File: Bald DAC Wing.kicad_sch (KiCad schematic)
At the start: 50 parts, among them J1 PWR, J10 Ctrl Debug, J2 DAC_A_Out, J3 DAC_B_Out, J5 Z_Out, J6 Feather, J7 Data Debug Low, J9 Data Debug High, U1 AD5447, U2 AD8065ARTZ, U3 AD8065ARTZ, U4 74LVC574APWR, U5 74LVC574APWR, U6 74LVC1G04, U7 REF3425

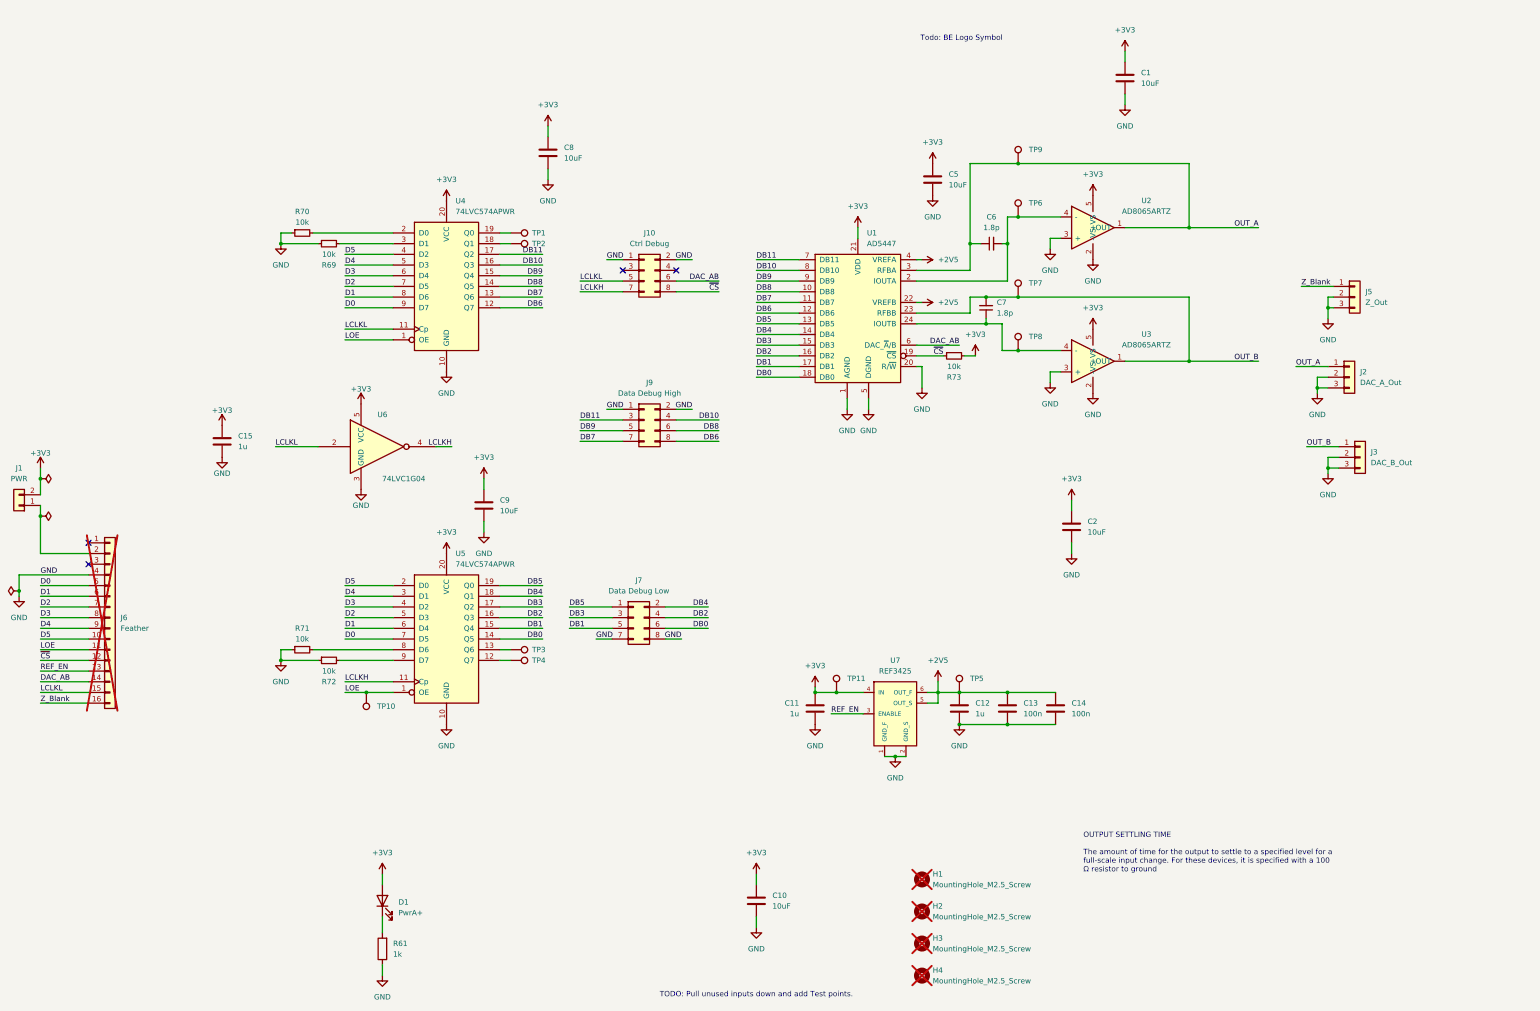
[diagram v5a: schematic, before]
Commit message: added BNCs for ABZ
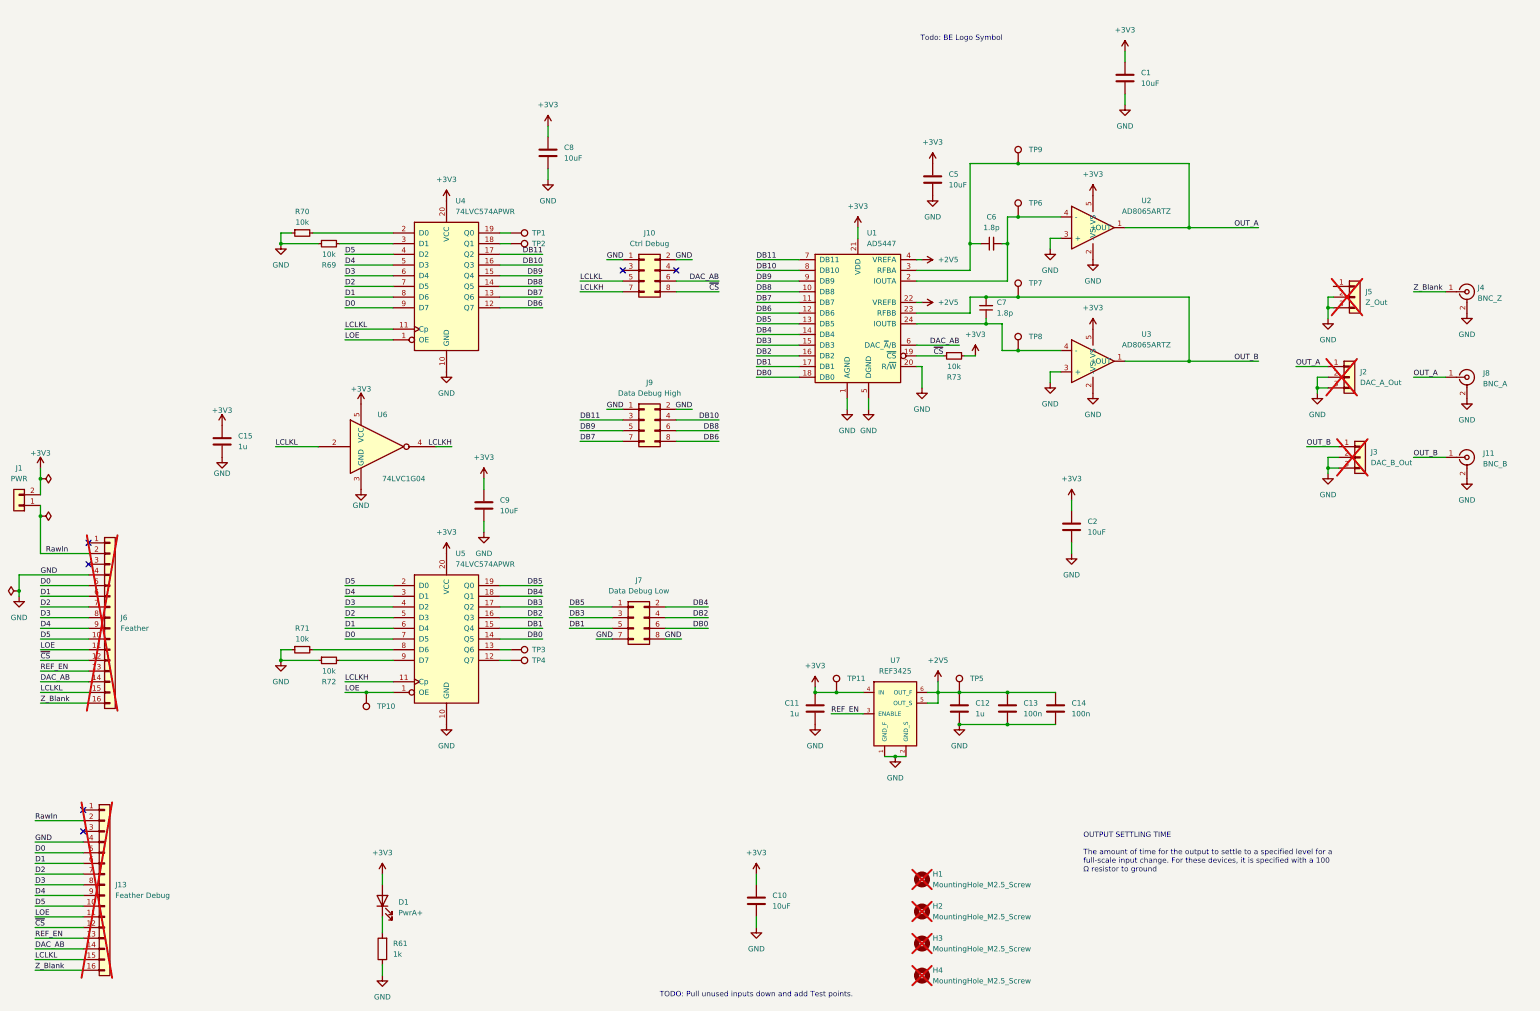
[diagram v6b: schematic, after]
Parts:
- added J11: BNC_B, My Libraries:Molex_73100-0105_BNC_RA, symbol Connector:Conn_Coaxial
- added J13: Feather Debug, Connector_PinSocket_2.54mm:PinSocket_1x16_P2.54mm_Vertical, symbol Connector_Generic:Conn_01x16
- added J4: BNC_Z, My Libraries:Molex_73100-0105_BNC_RA, symbol Connector:Conn_Coaxial
- added J8: BNC_A, My Libraries:Molex_73100-0105_BNC_RA, symbol Connector:Conn_Coaxial
- J2, J3, J5: now not fitted
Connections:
- net D0: now also J13.5 (Pin_5)
- net D1: now also J13.6 (Pin_6)
- net D2: now also J13.7 (Pin_7)
- net D3: now also J13.8 (Pin_8)
- net D4: now also J13.9 (Pin_9)
- net D5: now also J13.10 (Pin_10)
- net DAC_AB: now also J13.14 (Pin_14)
- net GND: now also J11.2 (Ext), J13.4 (Pin_4), J4.2 (Ext), J8.2 (Ext)
- net LCLKL: now also J13.15 (Pin_15)
- net LOE: now also J13.11 (Pin_11)
- net OUT_A: now also J8.1 (In)
- net OUT_B: now also J11.1 (In)
- net REF_EN: now also J13.13 (Pin_13)
- net Z_Blank: now also J13.16 (Pin_16), J4.1 (In); no longer J5.1 (Pin_1)
- net ~{CS}: now also J13.12 (Pin_12)
- net RawIn: now reaches J1.1 (Pin_1), J6.2 (Pin_2)
- net RawIn: now also J13.2 (Pin_2)
- no-connect marks 4 -> 6

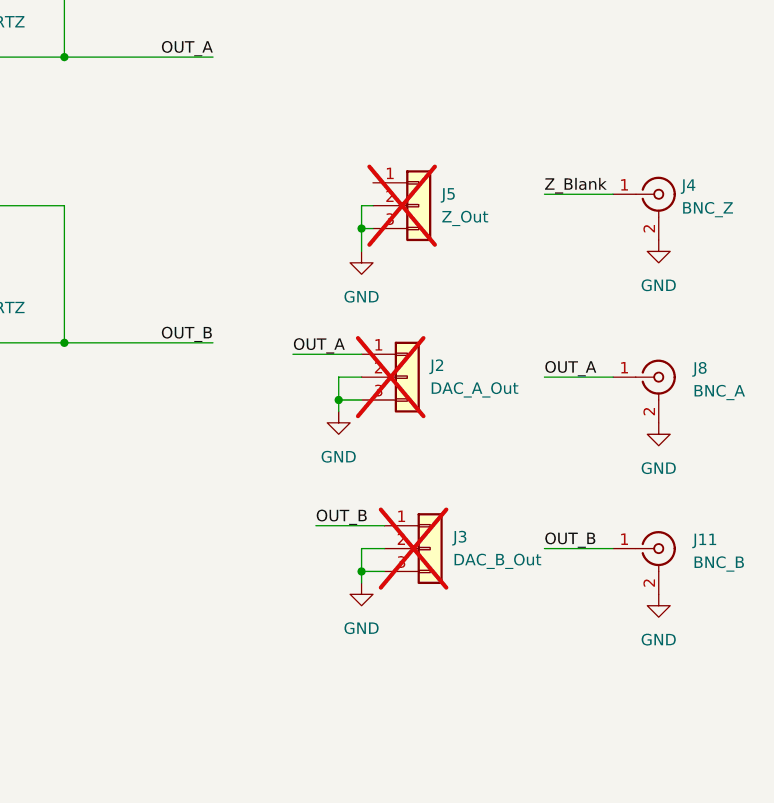
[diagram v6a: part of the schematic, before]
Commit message: added JLC constraints (imported from clanker template)
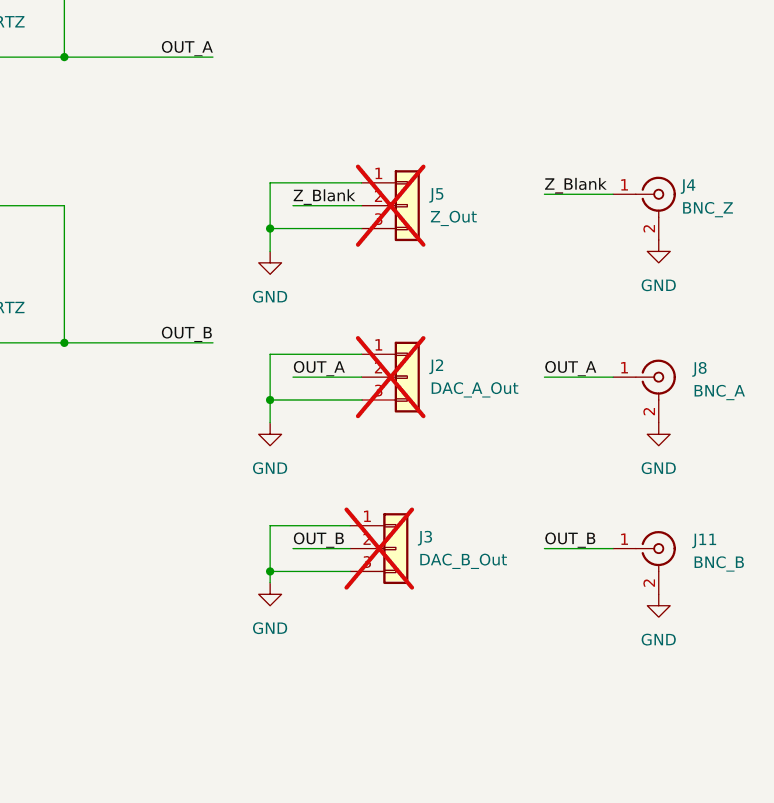
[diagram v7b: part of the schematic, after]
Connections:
- net GND: now also J2.1 (Pin_1), J3.1 (Pin_1), J5.1 (Pin_1); no longer J2.2 (Pin_2), J3.2 (Pin_2), J5.2 (Pin_2)
- net OUT_A: now also J2.2 (Pin_2); no longer J2.1 (Pin_1)
- net OUT_B: now also J3.2 (Pin_2); no longer J3.1 (Pin_1)
- net Z_Blank: now also J5.2 (Pin_2)
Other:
- moved on the sheet: J3, J5

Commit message: data buses are done. see optimizations, but going to finish
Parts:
- removed R70, R71: 10k, Resistor_SMD:R_0603_1608Metric_Pad0.98x0.95mm_HandSolder, symbol Device:R_Small
- removed TP1, TP2, TP3, TP4: TestPoint_Harwin, My Libraries:Harwin-S1751-46-Test-Point, symbol My Library:TestPoint_Harwin
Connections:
- net at U4.2 (D0): now also R69.2, U4.3 (D1)
- net at R72.2, U5.9 (D7): now also U5.8 (D6)
- no-connect marks 6 -> 10
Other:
- moved on the sheet: R69
